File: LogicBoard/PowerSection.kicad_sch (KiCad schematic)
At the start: 30 parts, among them U2 TPS65150PWPR

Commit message: added jlcpcb nums to some parts
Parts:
- added R9: 0R, Resistor_SMD:R_1206_3216Metric_Pad1.30x1.75mm_HandSolder, symbol Device:R
- C1, C11, C12, C2: footprint (none) -> Capacitor_SMD:C_0603_1608Metric; jlcpcbpart (none) -> C1615
- C10, C13: footprint (none) -> Capacitor_SMD:C_0603_1608Metric; jlcpcbpart (none) -> C15849
- C14: footprint (none) -> Capacitor_SMD:C_0805_2012Metric; jlcpcbpart (none) -> C45783
- C15, C7: footprint (none) -> Capacitor_SMD:C_0402_1005Metric; jlcpcbpart (none) -> C1555
- C16: footprint (none) -> Capacitor_SMD:C_0603_1608Metric; jlcpcbpart (none) -> C14663
- C3: footprint (none) -> Capacitor_SMD:C_0402_1005Metric; jlcpcbpart (none) -> C16772
- C5, C6: footprint (none) -> Capacitor_SMD:C_0402_1005Metric; jlcpcbpart (none) -> C15195
- C8, C9: footprint (none) -> Capacitor_SMD:C_0402_1005Metric; jlcpcbpart (none) -> C1531
- D1, D2, D3, D4, D5: footprint Diode_THT:D_DO-41_SOD81_P10.16mm_Horizontal -> Diode_SMD:D_SOD-123F; jlcpcbpart (none) -> C437955
- L1: footprint (none) -> Inductor_SMD:L_Changjiang_FNR8040S; jlcpcbpart (none) -> C168120
- R1, R3, R4: value 500k -> 510k; footprint (none) -> Resistor_SMD:R_0402_1005Metric; jlcpcbpart (none) -> C11616
- R2: footprint (none) -> Resistor_SMD:R_0402_1005Metric; jlcpcbpart (none) -> C25741
- R5: footprint (none) -> Resistor_SMD:R_0402_1005Metric; jlcpcbpart (none) -> C26083
- R6: footprint (none) -> Resistor_SMD:R_0402_1005Metric; jlcpcbpart (none) -> C25798
- R7: footprint (none) -> Resistor_SMD:R_0402_1005Metric; jlcpcbpart (none) -> C36871
- R8: footprint (none) -> Resistor_SMD:R_0402_1005Metric; jlcpcbpart (none) -> C11616
- U2: jlcpcbpart (none) -> C140349
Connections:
- net +5V_I: now also R9.1
- net at U2.13 (CTRL): now also R9.2
- net LED_A renamed +9.6V
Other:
- note added: "510k / 100k = -6.100V"
- note removed: "500k / 100k = -6.065V"

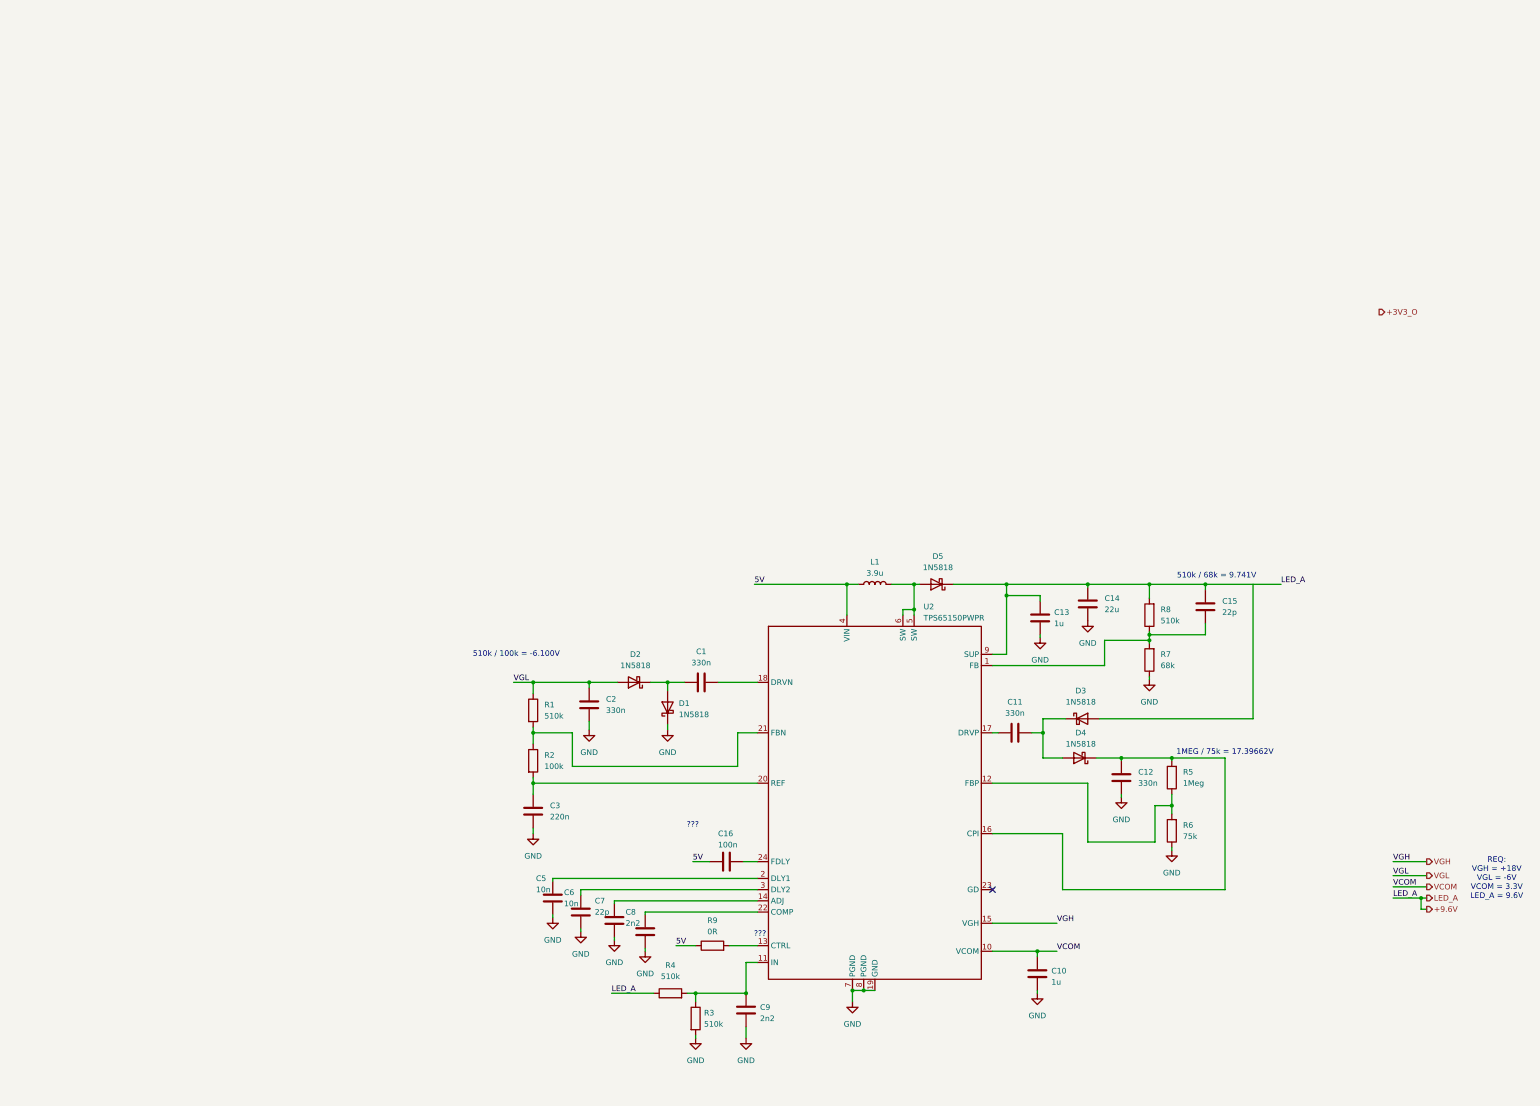
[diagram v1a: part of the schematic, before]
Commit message: lcd schematic now matches requirement, added 3v3 dcdc stage for MCUs
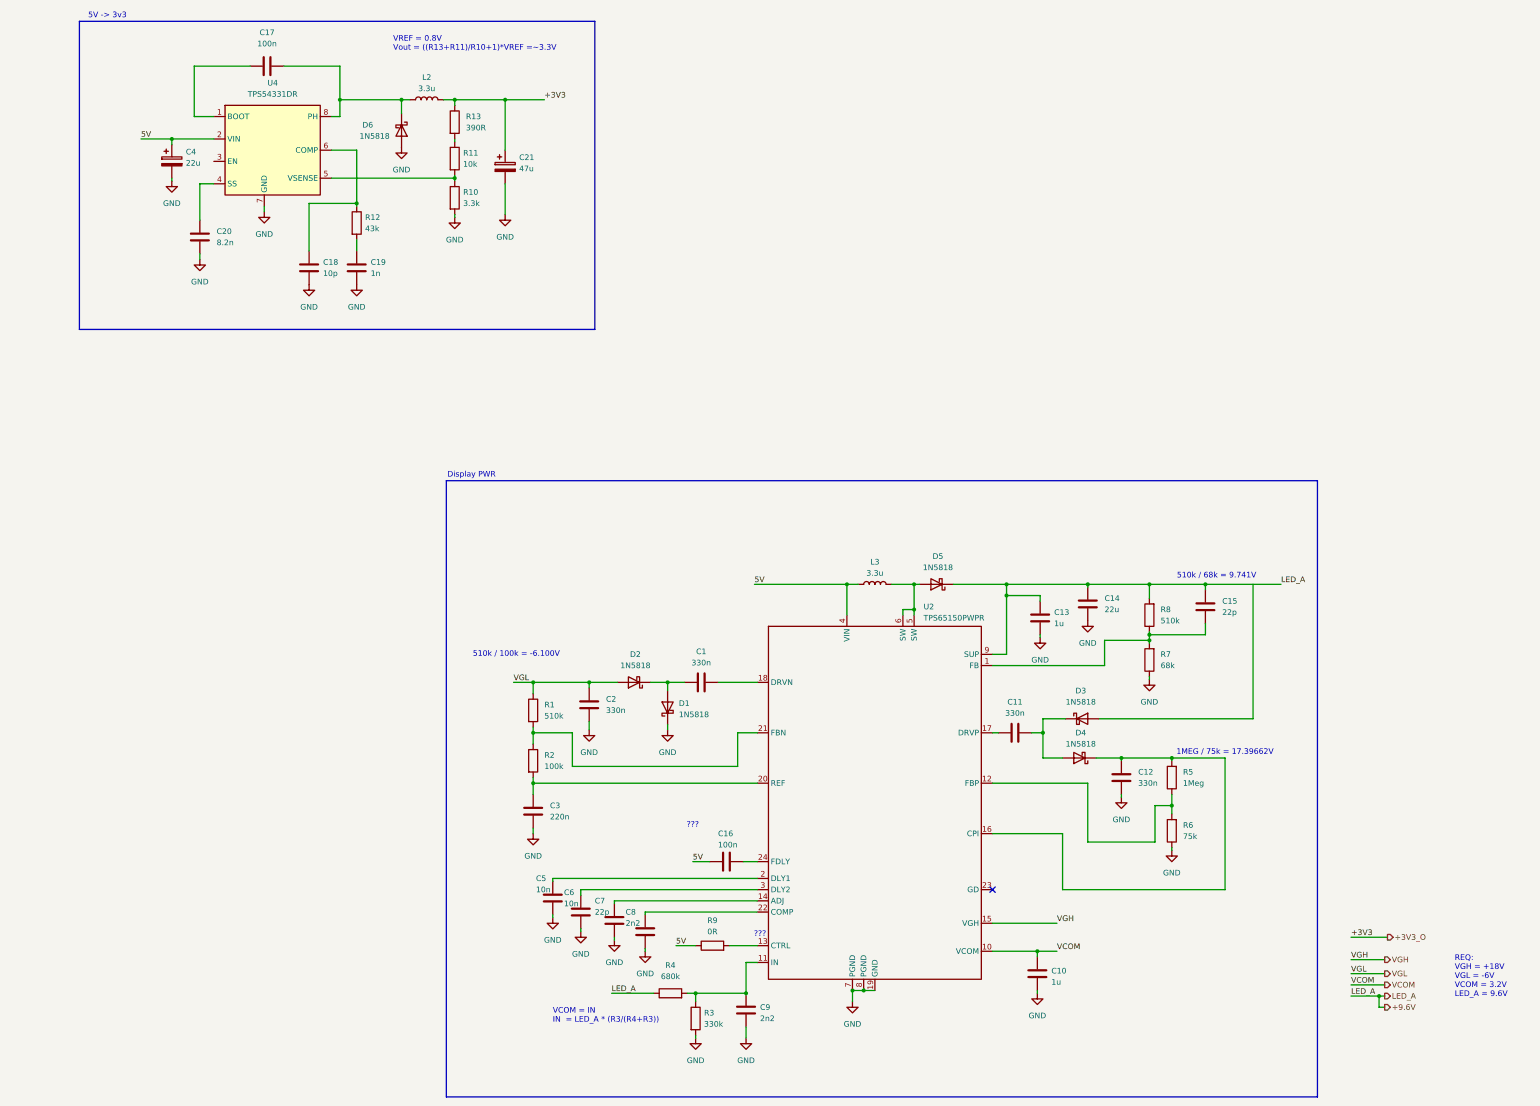
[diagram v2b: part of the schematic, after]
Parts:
- removed L1: 3.9u, Inductor_SMD:L_Changjiang_FNR8040S, symbol Device:L
- added C17: 100n, Capacitor_SMD:C_0603_1608Metric, symbol Device:C
- added C18: 10p, Capacitor_SMD:C_0402_1005Metric, symbol Device:C
- added C19: 1n, Capacitor_SMD:C_0402_1005Metric, symbol Device:C
- added C20: 8.2n, Capacitor_SMD:C_0603_1608Metric, symbol Device:C
- added C21: 47u, Capacitor_SMD:CP_Elec_5x5.3, symbol Device:C_Polarized
- added C4: 22u, symbol Device:C_Polarized
- added D6: 1N5818, Diode_SMD:D_SOD-123F, symbol Diode:1N5818
- added L2, L3: 3.3u, Inductor_SMD:L_Changjiang_FNR8065S, symbol Device:L
- added R10: 3.3k, Resistor_SMD:R_0402_1005Metric, symbol Device:R
- added R11: 10k, Resistor_SMD:R_0402_1005Metric, symbol Device:R
- added R12: 43k, Resistor_SMD:R_0603_1608Metric, symbol Device:R
- added R13: 390R, Resistor_SMD:R_0603_1608Metric, symbol Device:R
- added U4: TPS54331DR, Package_SO:SOIC-8_3.9x4.9mm_P1.27mm, symbol dcdc:TPS54331DR
- R3: value 510k -> 330k; jlcpcbpart C11616 -> C25778
- R4: value 510k -> 680k; footprint Resistor_SMD:R_0402_1005Metric -> Resistor_SMD:R_0603_1608Metric; jlcpcbpart C11616 -> C25822
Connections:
- net +3V3_O: now also C21.1, L2.2, R13.1
- net +5V_I: now also C4.1, L3.1, U4.2 (VIN)
- net GND: now also C18.2, C19.2, C20.2, C21.2, C4.2, D6.2 (A), R10.2, U4.7 (GND)
- net at D5.2 (A), U2.5 (SW), U2.6 (SW): now also L3.2
- new net: R11.1, R13.2
- new net: C18.1, R12.1, U4.6 (COMP)
- new net: C19.1, R12.2
- new net: R10.1, R11.2, U4.5 (VSENSE)
- new net: C17.1, D6.1 (K), L2.1, U4.8 (PH)
- new net: C17.2, U4.1 (BOOT)
- new net: C20.1, U4.4 (SS)
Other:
- note added: "5V -> 3v3"
- note added: "Display PWR"
- note added: "REQ: VGH = +18V VGL = -6V VCOM = 3.2V LED_A = 9.6V"
- note added: "VCOM = IN IN = LED_A * (R3/(R4+R3))"
- note added: "VREF = 0.8V Vout = ((R13+R11)/R10+1)*VREF =~3.3V"
- note removed: "REQ: VGH = +18V VGL = -6V VCOM = 3.3V LED_A = 9.6V"

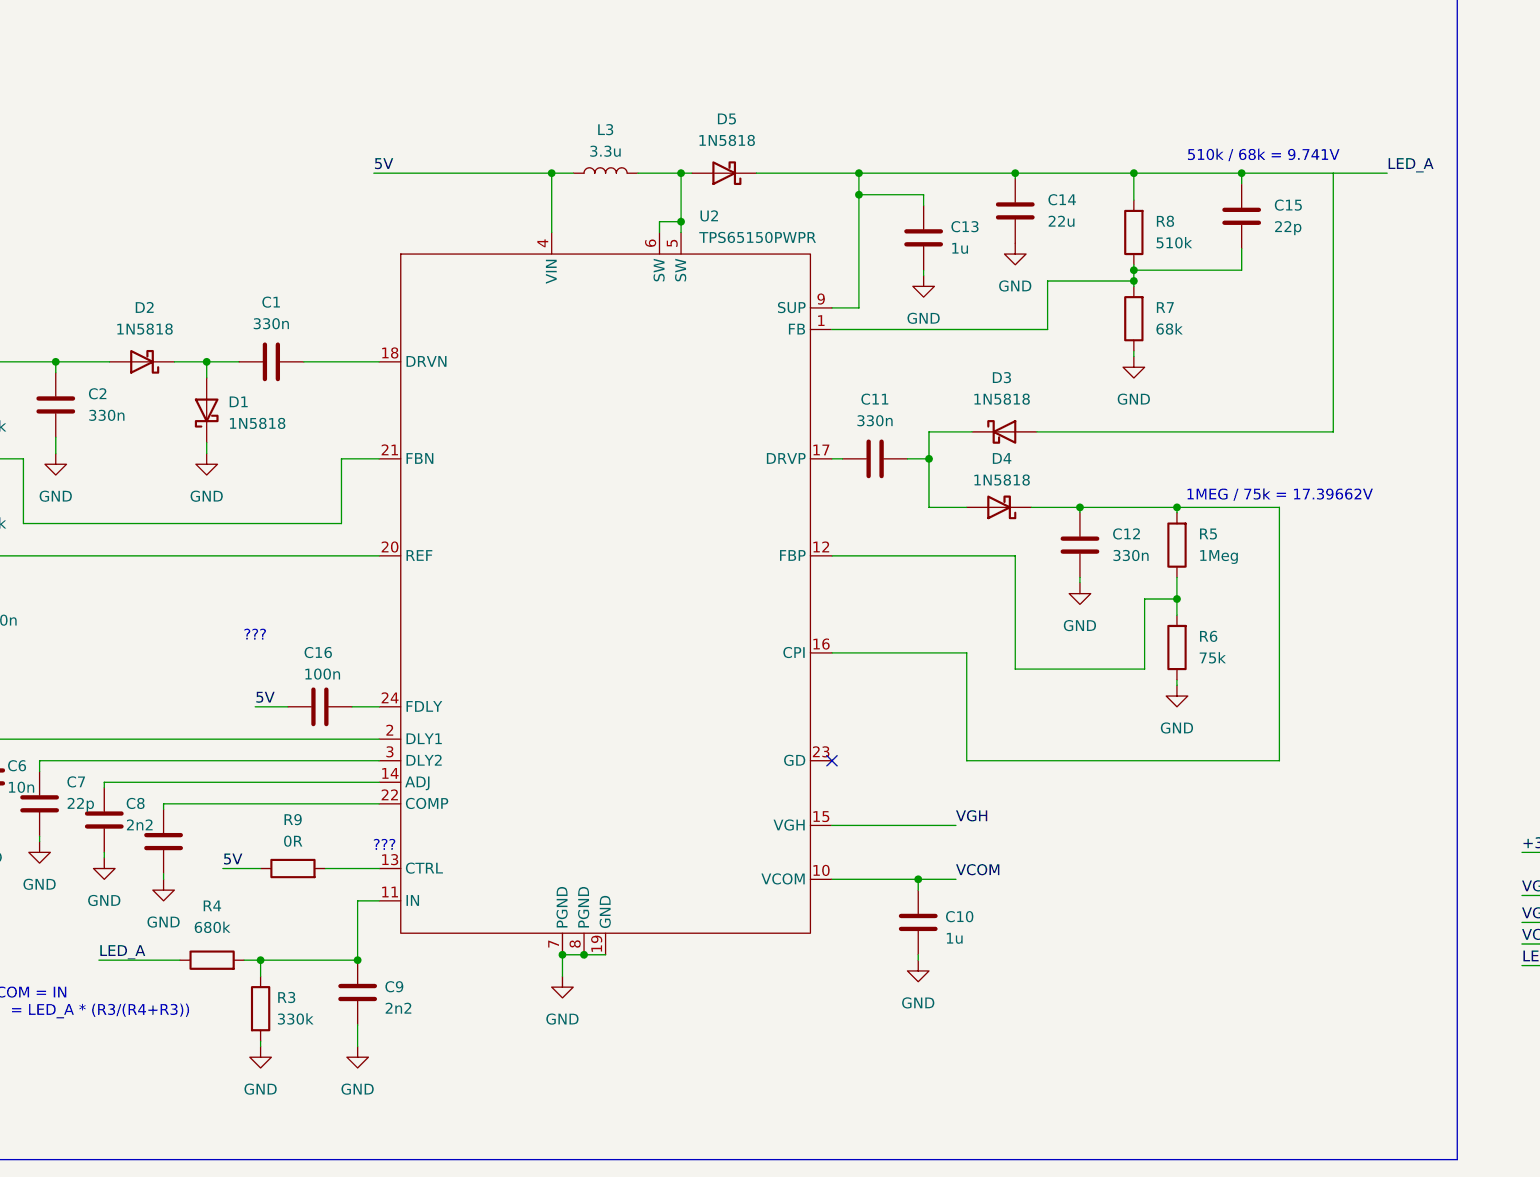
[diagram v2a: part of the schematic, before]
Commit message: Created display psu layout
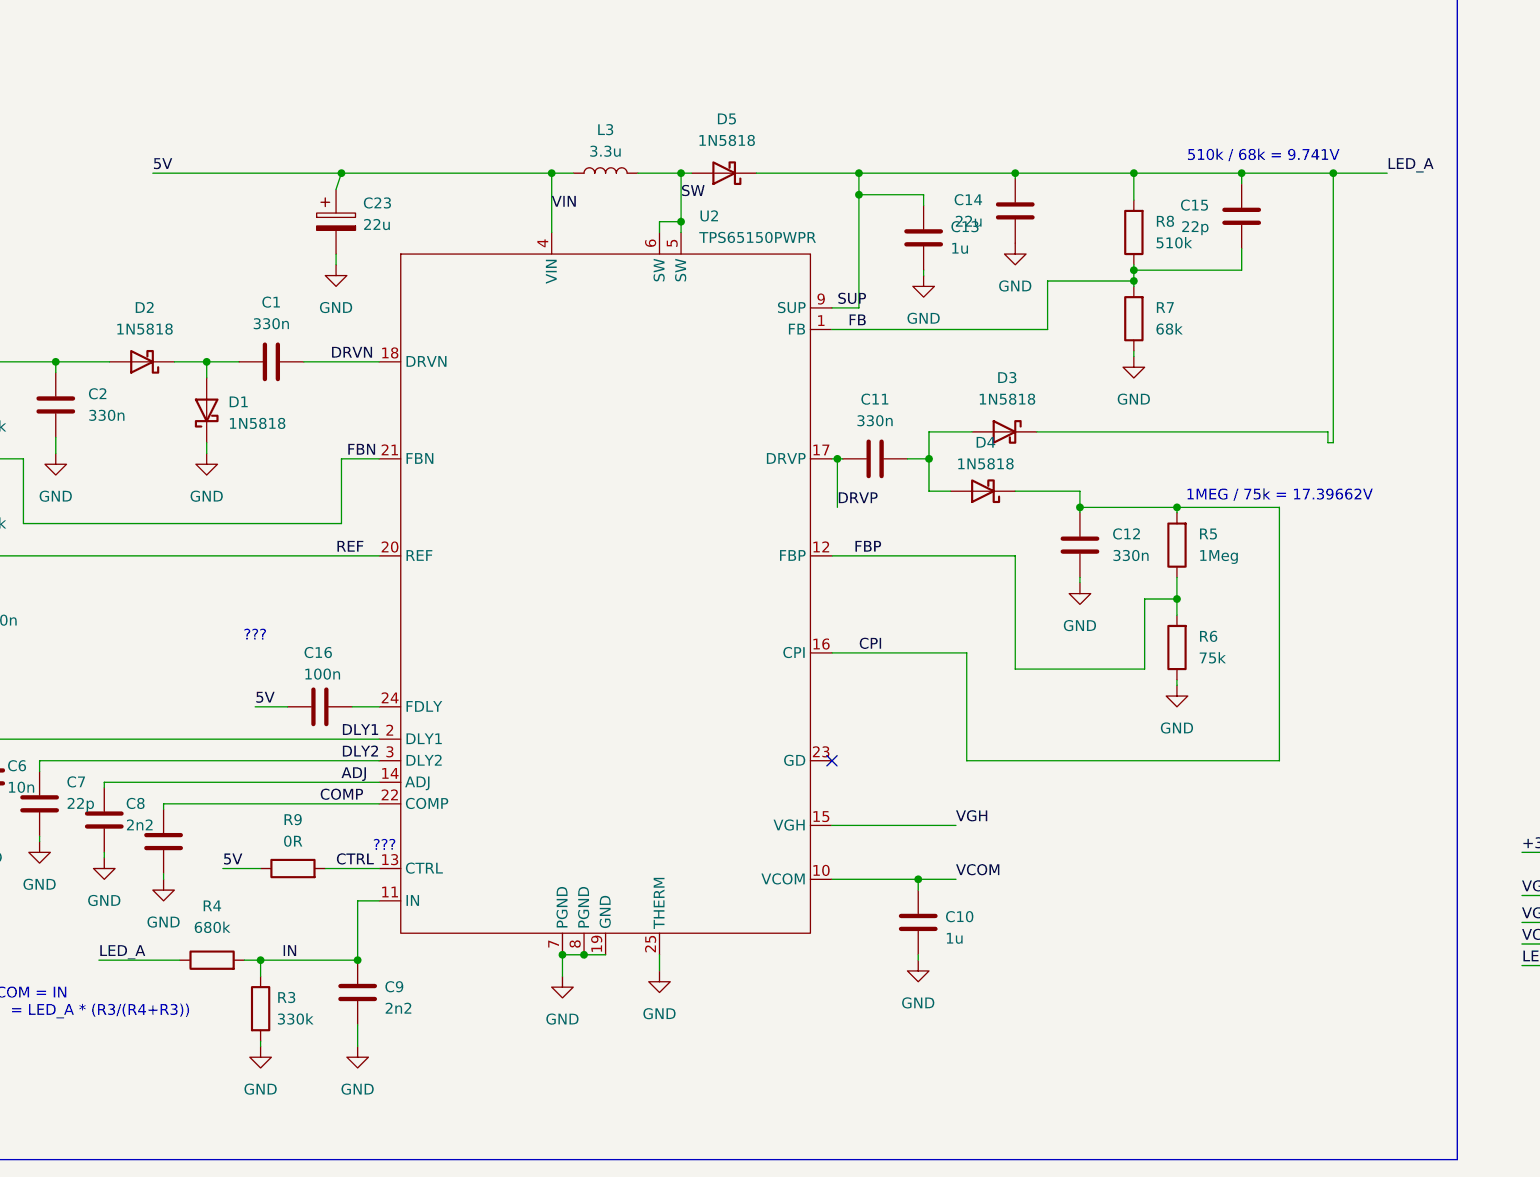
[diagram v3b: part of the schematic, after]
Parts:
- added C23: 22u, Capacitor_SMD:CP_Elec_5x5.4, symbol Device:C_Polarized
- C4: footprint (none) -> Capacitor_SMD:CP_Elec_5x5.4; jlcpcbpart (none) -> C5444307
- L2, L3: jlcpcbpart (none) -> C168157
- U2: footprint Package_SO:HTSSOP-24-1EP_4.4x7.8mm_P0.65mm_EP3.4x7.8mm_Mask2.44x3.42mm_ThermalVias -> Package_SO:HTSSOP-24-1EP_4.4x7.8mm_P0.65mm_EP3.4x7.8mm_Mask2.4x4.68mm_ThermalVias
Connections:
- net +5V_I: now also C23.1
- net +9.6V: now also D3.1 (K)
- net GND: now also U2.25 (THERM), C23.2
- net CTRL: now reaches R9.2, U2.13 (CTRL)
- net ADJ: now reaches C7.1, U2.14 (ADJ)
- net FB: now reaches C15.2, R7.2, R8.1, U2.1 (FB)
- net FBP: now reaches R5.1, R6.2, U2.12 (FBP)
- net REF: now reaches C3.2, R2.2, U2.20 (REF)
- net FBN: now reaches R1.2, R2.1, U2.21 (FBN)
- net at C11.1, D4.2 (A): now also D3.2 (A); no longer D3.1 (K)
- net CPI: now reaches C12.1, D4.1 (K), R5.2, U2.16 (CPI)
- net DRVN: now reaches C1.2, U2.18 (DRVN)
- net SW: now reaches D5.2 (A), L3.2, U2.5 (SW), U2.6 (SW)
- net IN: now reaches C9.1, R3.1, R4.2, U2.11 (IN)
- net DLY2: now reaches C6.1, U2.3 (DLY2)
- net DLY1: now reaches C5.1, U2.2 (DLY1)
- net DRVP: now reaches C11.2, U2.17 (DRVP)
- net COMP: now reaches C8.1, U2.22 (COMP)
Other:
- moved on the sheet: D4
